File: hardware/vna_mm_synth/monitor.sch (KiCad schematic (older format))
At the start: 18 parts

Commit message: work on mm synth io lines
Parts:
- R1206, R1207, R1208, R1209, R1210, R1211: renamed from R?; footprint (none) -> Resistor_SMD:R_0402_1005Metric
- gave numbers to parts that had none: 12

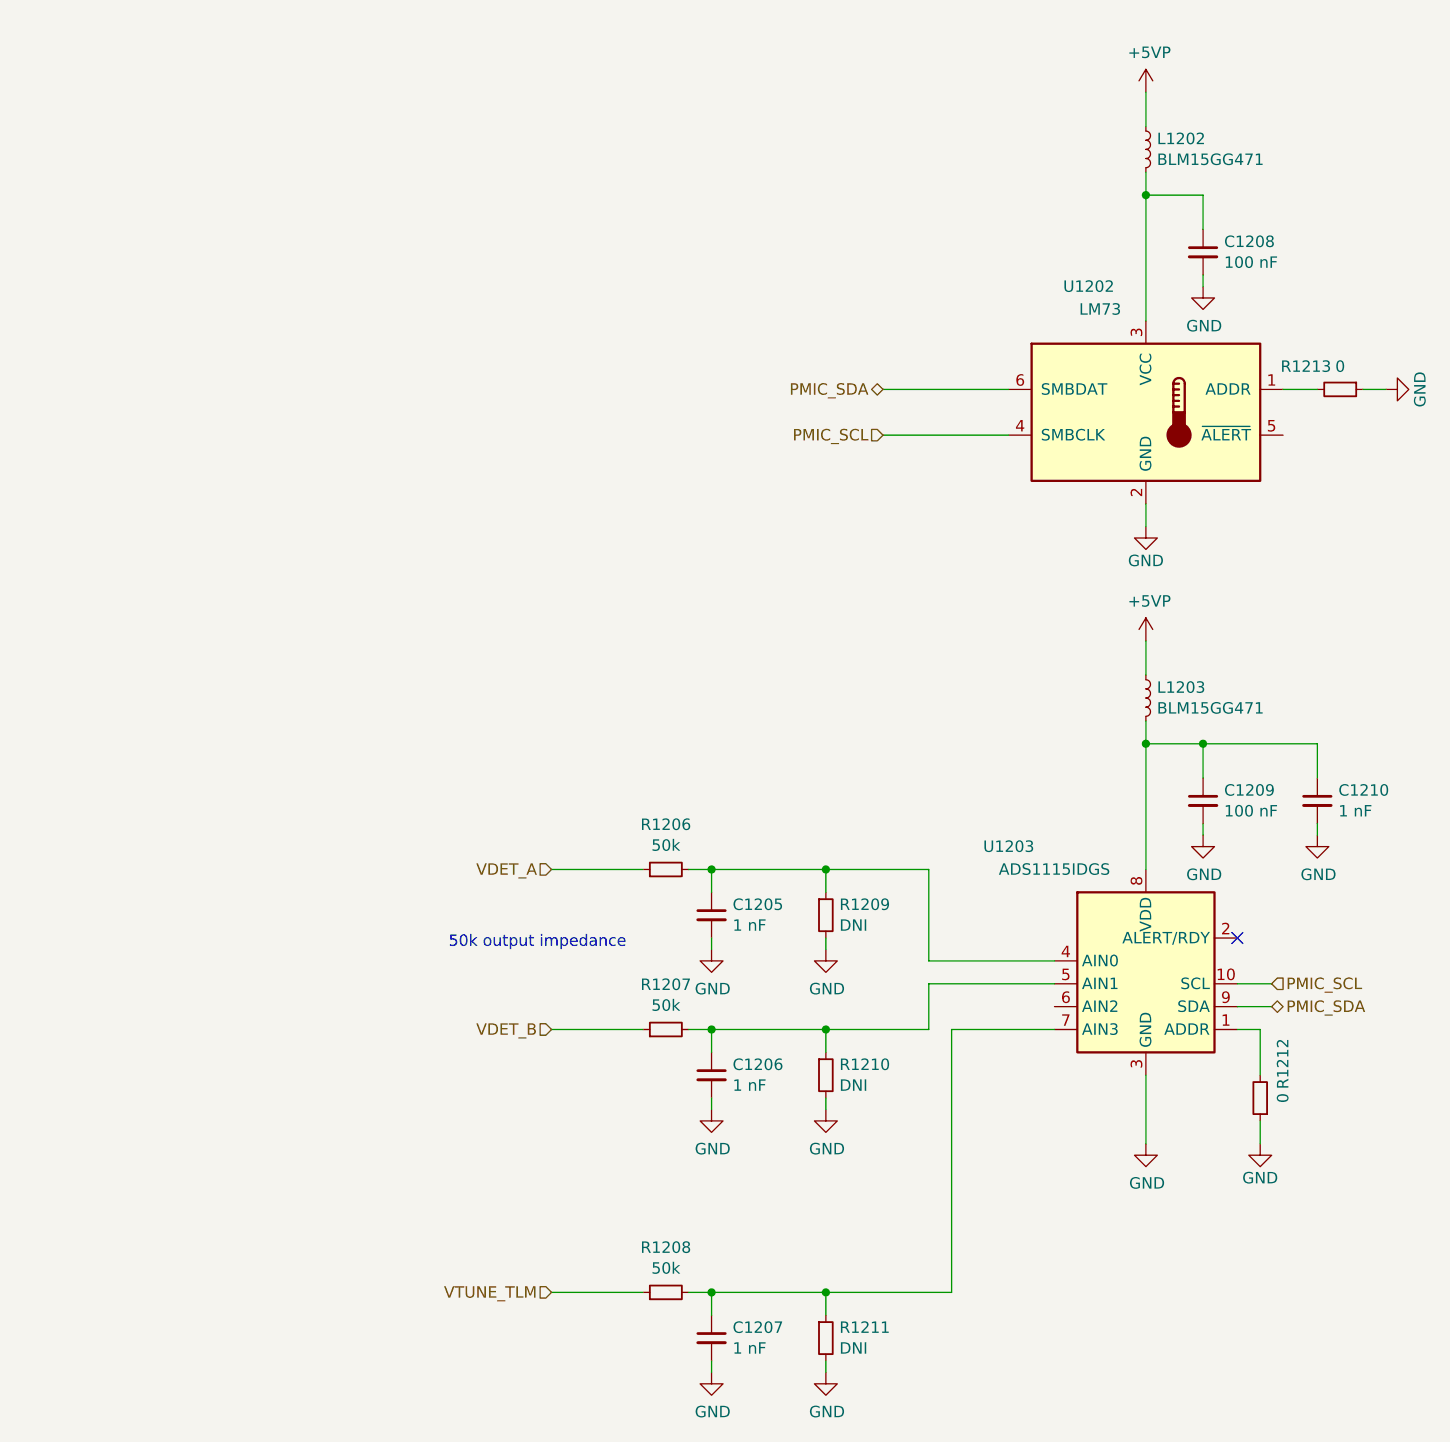
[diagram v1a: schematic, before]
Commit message: added buffers to digital inputs on mm synth
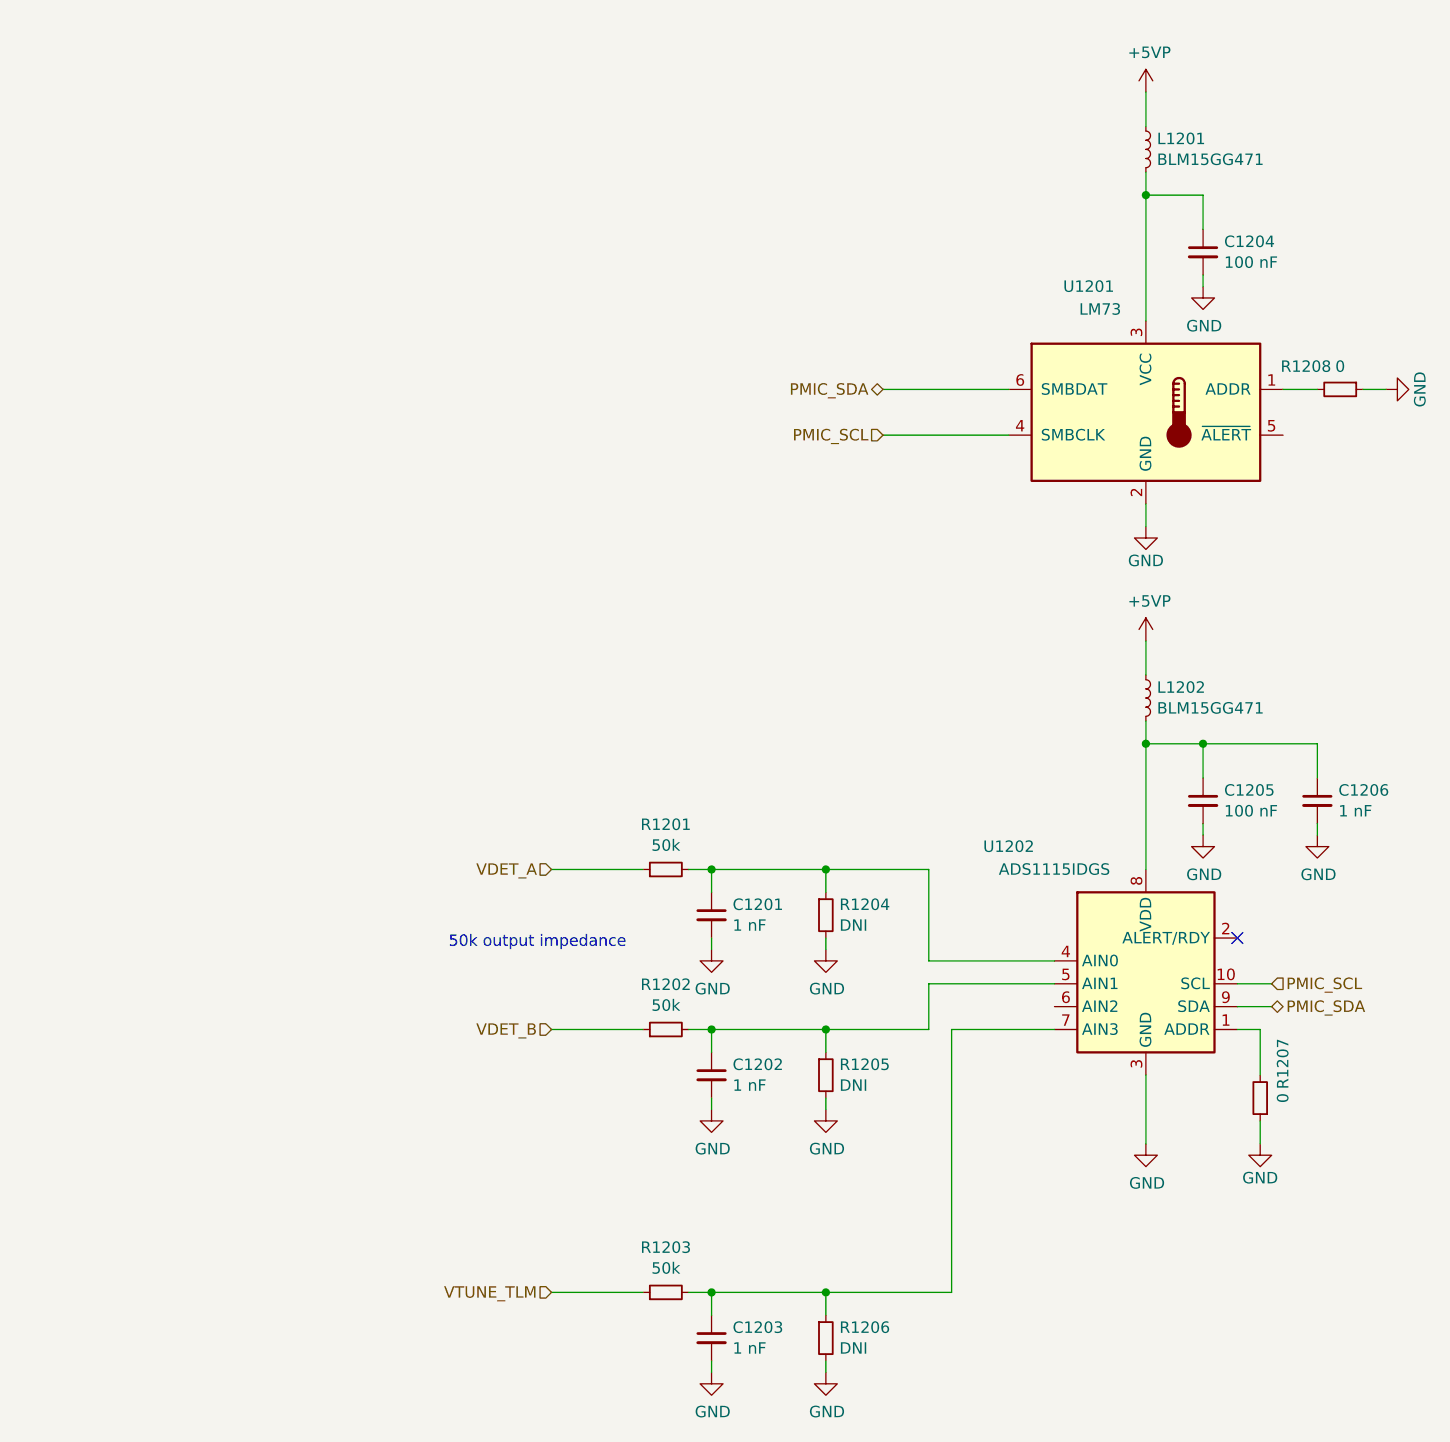
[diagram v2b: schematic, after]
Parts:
- renumbered C1205 to C1201, C1206 to C1202, C1207 to C1203, C1208 to C1204, C1209 to C1205, C1210 to C1206, L1202 to L1201, L1203 to L1202, R1206 to R1201, R1207 to R1202, R1208 to R1203, R1209 to R1204, R1210 to R1205, R1211 to R1206, R1212 to R1207, R1213 to R1208, U1202 to U1201, U1203 to U1202

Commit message: work on vna mm synth digital lines, added i2c eeprom
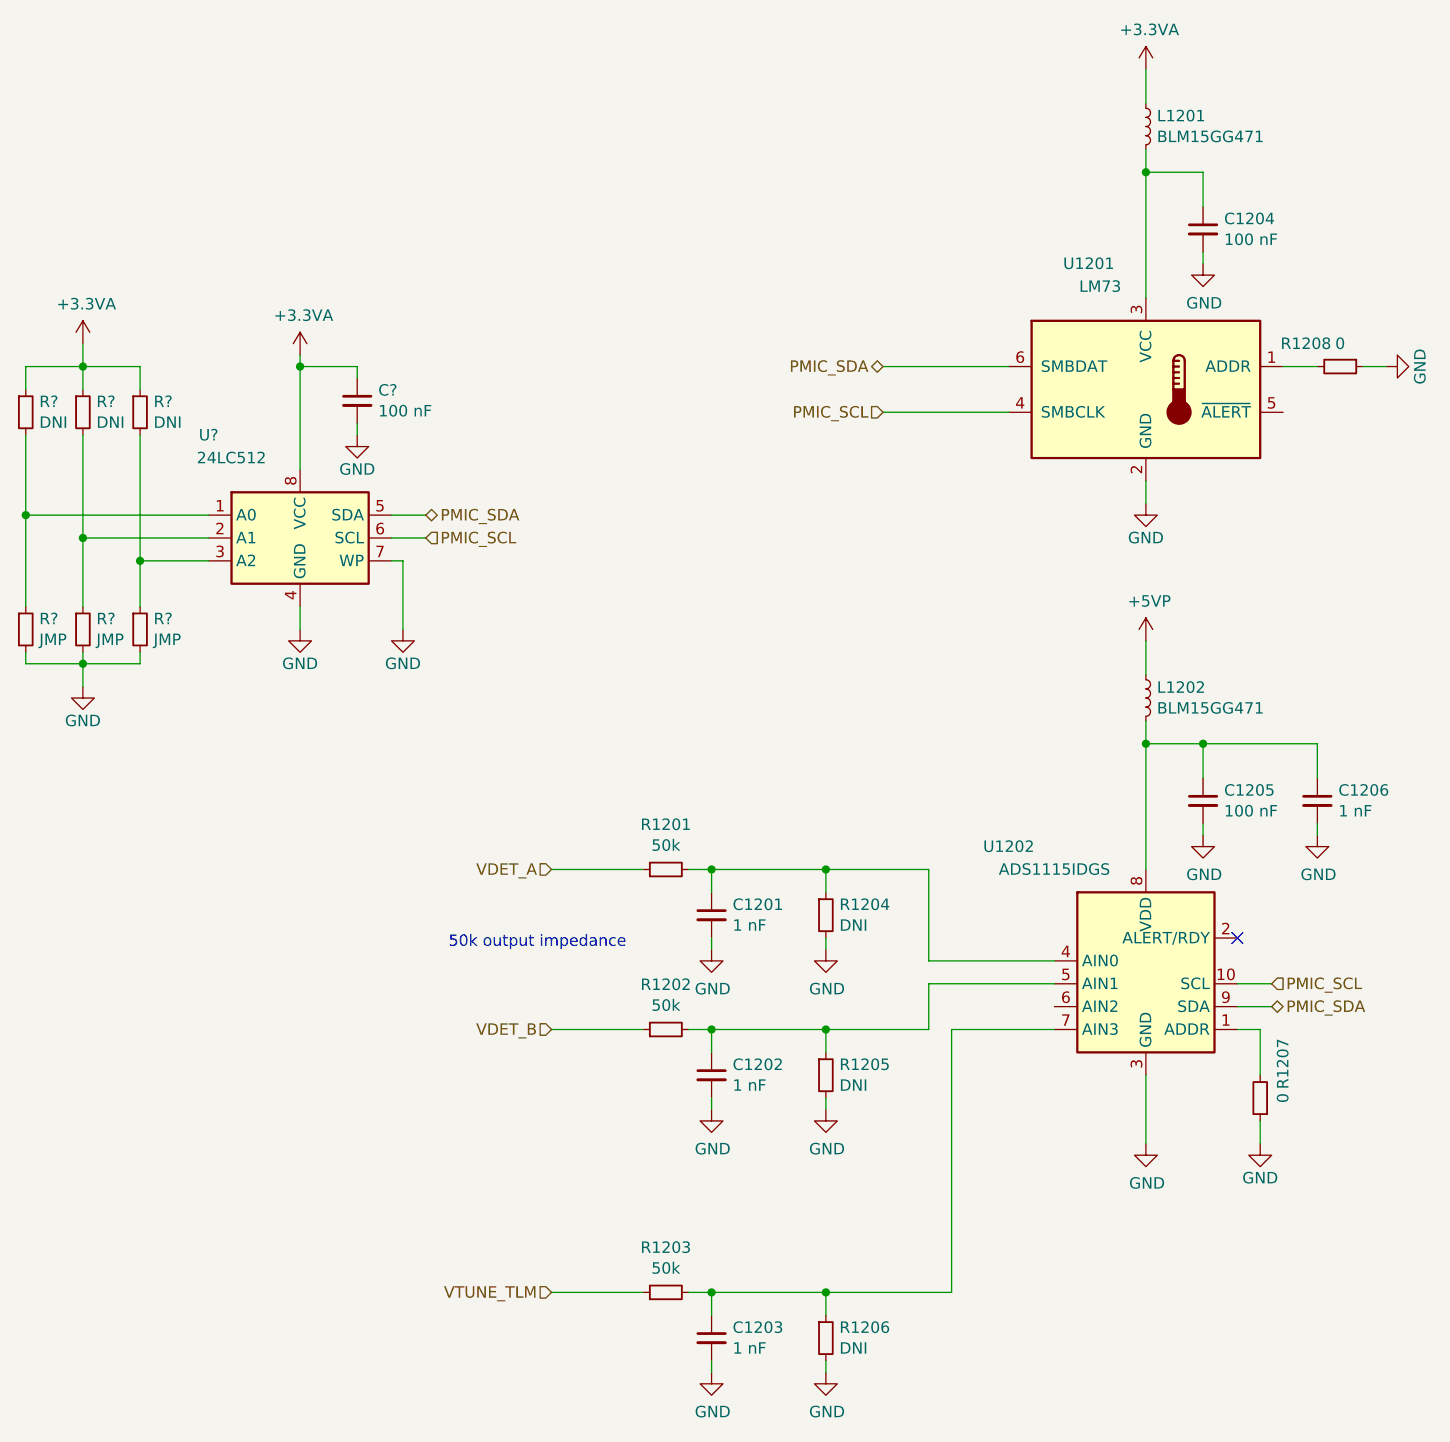
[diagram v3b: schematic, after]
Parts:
- added C?: 100 nF, symbol Device:C_Small
- added R? (x3): JMP, Resistor_SMD:R_0402_1005Metric, symbol Device:R_Small
- added R? (x3): DNI, Resistor_SMD:R_0402_1005Metric, symbol Device:R_Small
- added U?: 24LC512, symbol Memory_EEPROM:24LC512
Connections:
- net +5VP: no longer L1201.1
- net GND: now also C?.2, R?.2, R?.2, R?.2, U?.4 (GND), U?.7 (WP)
- net PMIC_SCL: now also U?.6 (SCL)
- net PMIC_SDA: now also U?.5 (SDA)
- new net: R?.1, R?.2, U?.1 (A0)
- new net: R?.1, R?.2, U?.2 (A1)
- new net: R?.1, R?.2, U?.3 (A2)
- new net +3.3VA: C?.1, L1201.1, R?.1, R?.1, R?.1, U?.8 (VCC)
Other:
- moved on the sheet: C1204, L1201, R1208, U1201

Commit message: finished first pass at schematic, starting mm synth layout
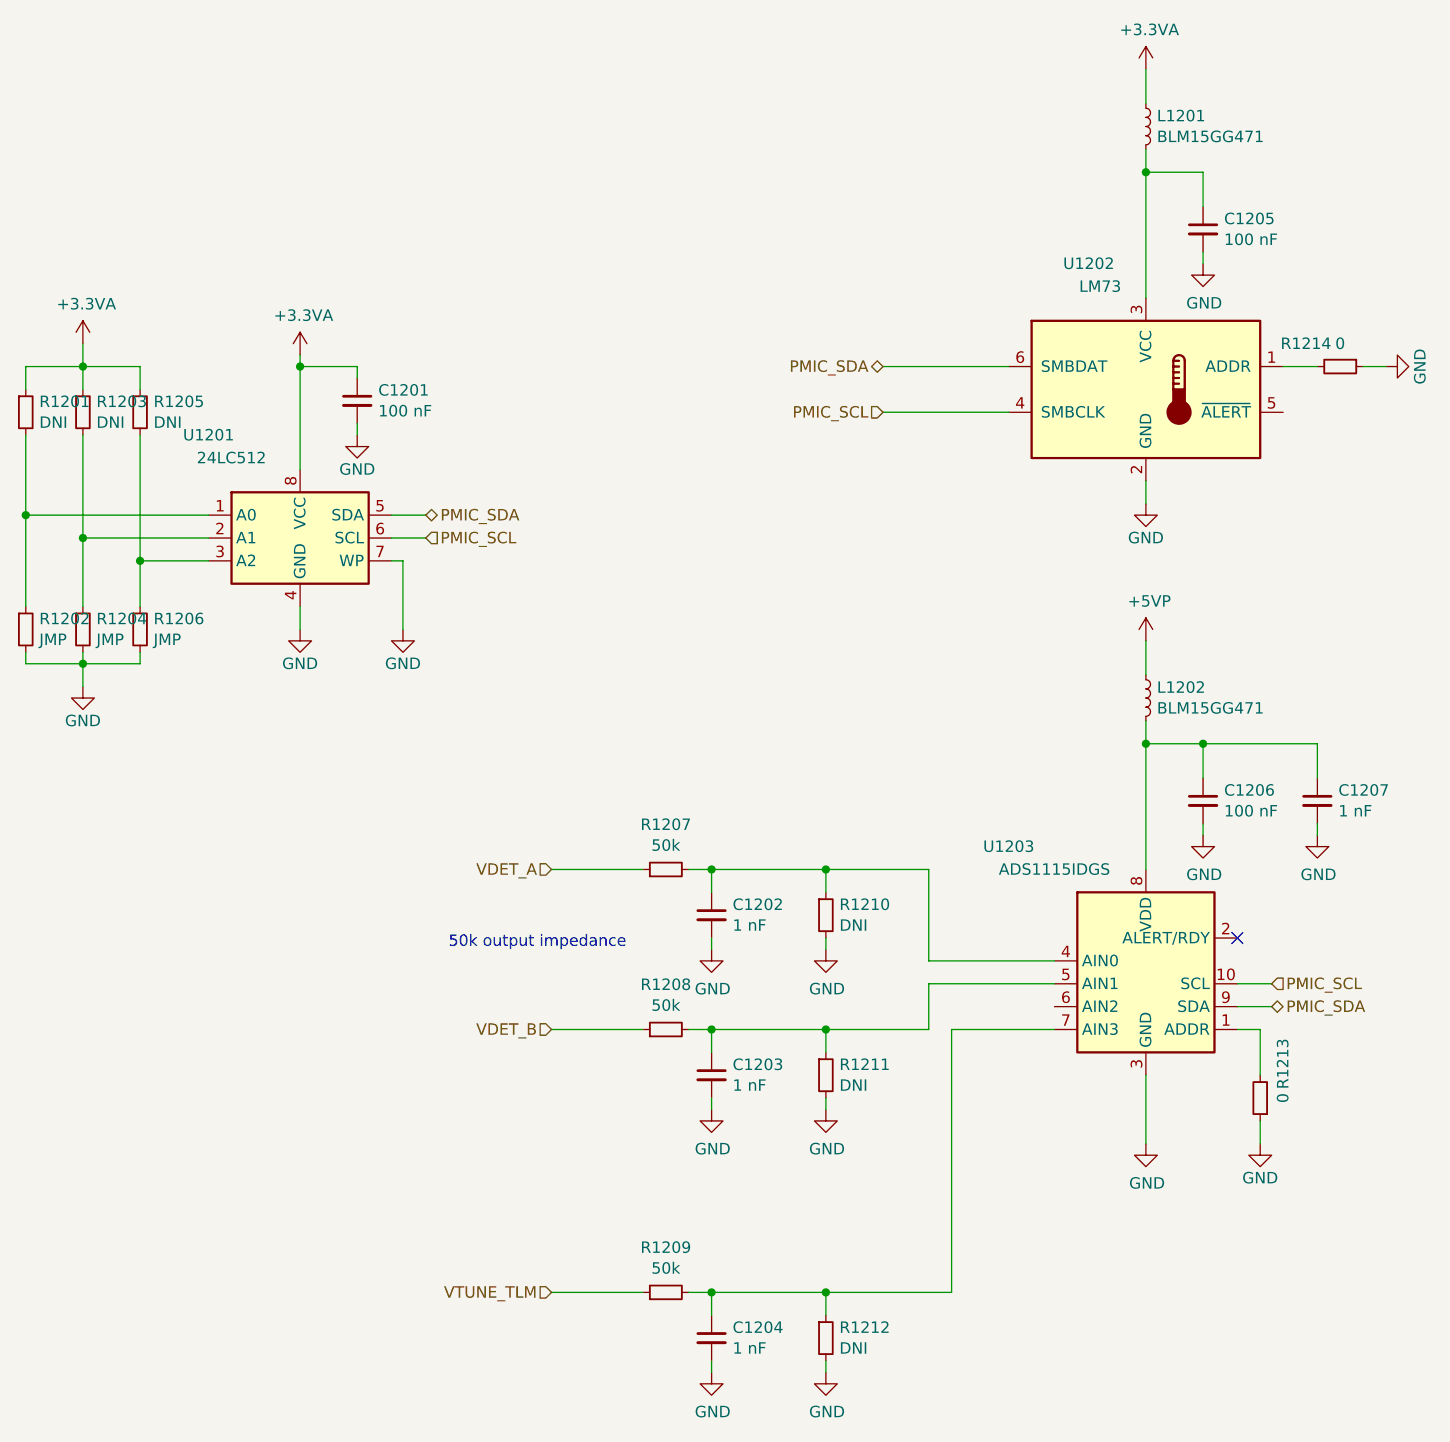
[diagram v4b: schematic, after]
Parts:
- C1201: renamed from C?; footprint (none) -> Capacitor_SMD:C_0402_1005Metric
- U1201: renamed from U?; footprint (none) -> Package_SO:TSSOP-8_4.4x3mm_P0.65mm
- gave numbers to parts that had none: 6
- renumbered C1201 to C1202, C1202 to C1203, C1203 to C1204, C1204 to C1205, C1205 to C1206, C1206 to C1207, R1201 to R1207, R1202 to R1208, R1203 to R1209, R1204 to R1210, R1205 to R1211, R1206 to R1212, R1207 to R1213, R1208 to R1214, U1201 to U1202, U1202 to U1203

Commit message: fix vna mm synth erc errors
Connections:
- no-connect marks 1 -> 3
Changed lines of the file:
@@
 	1550 3400 1550 3600
 Connection ~ 1550 3400
+NoConn ~ 5550 5350
+NoConn ~ 6550 2750
 $EndSCHEMATC
